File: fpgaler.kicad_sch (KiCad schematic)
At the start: 66 parts, among them J1 USB_C_Receptacle_USB2.0, J2 BATT, J3 JTAG, J4 FTDI_RST, J5 VGA, J6 DB9 Expander, SW1 RotaryEncoder_Switch, SW2 RotaryEncoder_Switch, SW3 K1, SW4 K2, SW5 PROGRAMN, SW6 K3, SW7 FPGA GSRN, SW8 K4

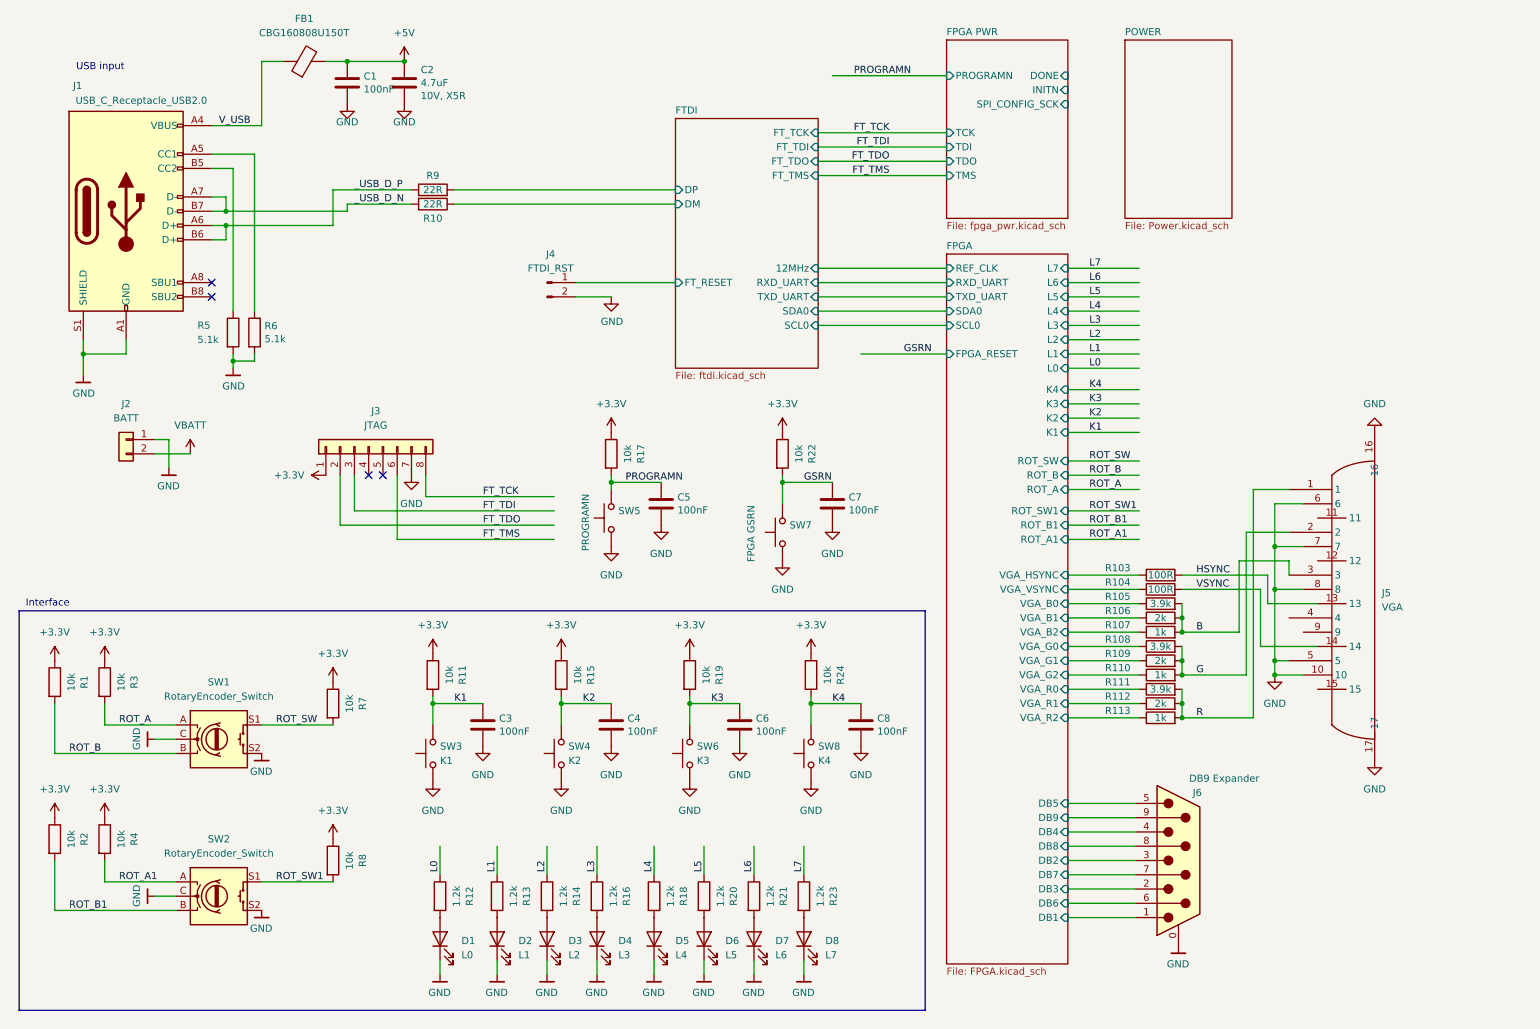
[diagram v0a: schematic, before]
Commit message: Place db9, encoder, btn and leds. Continue routing.
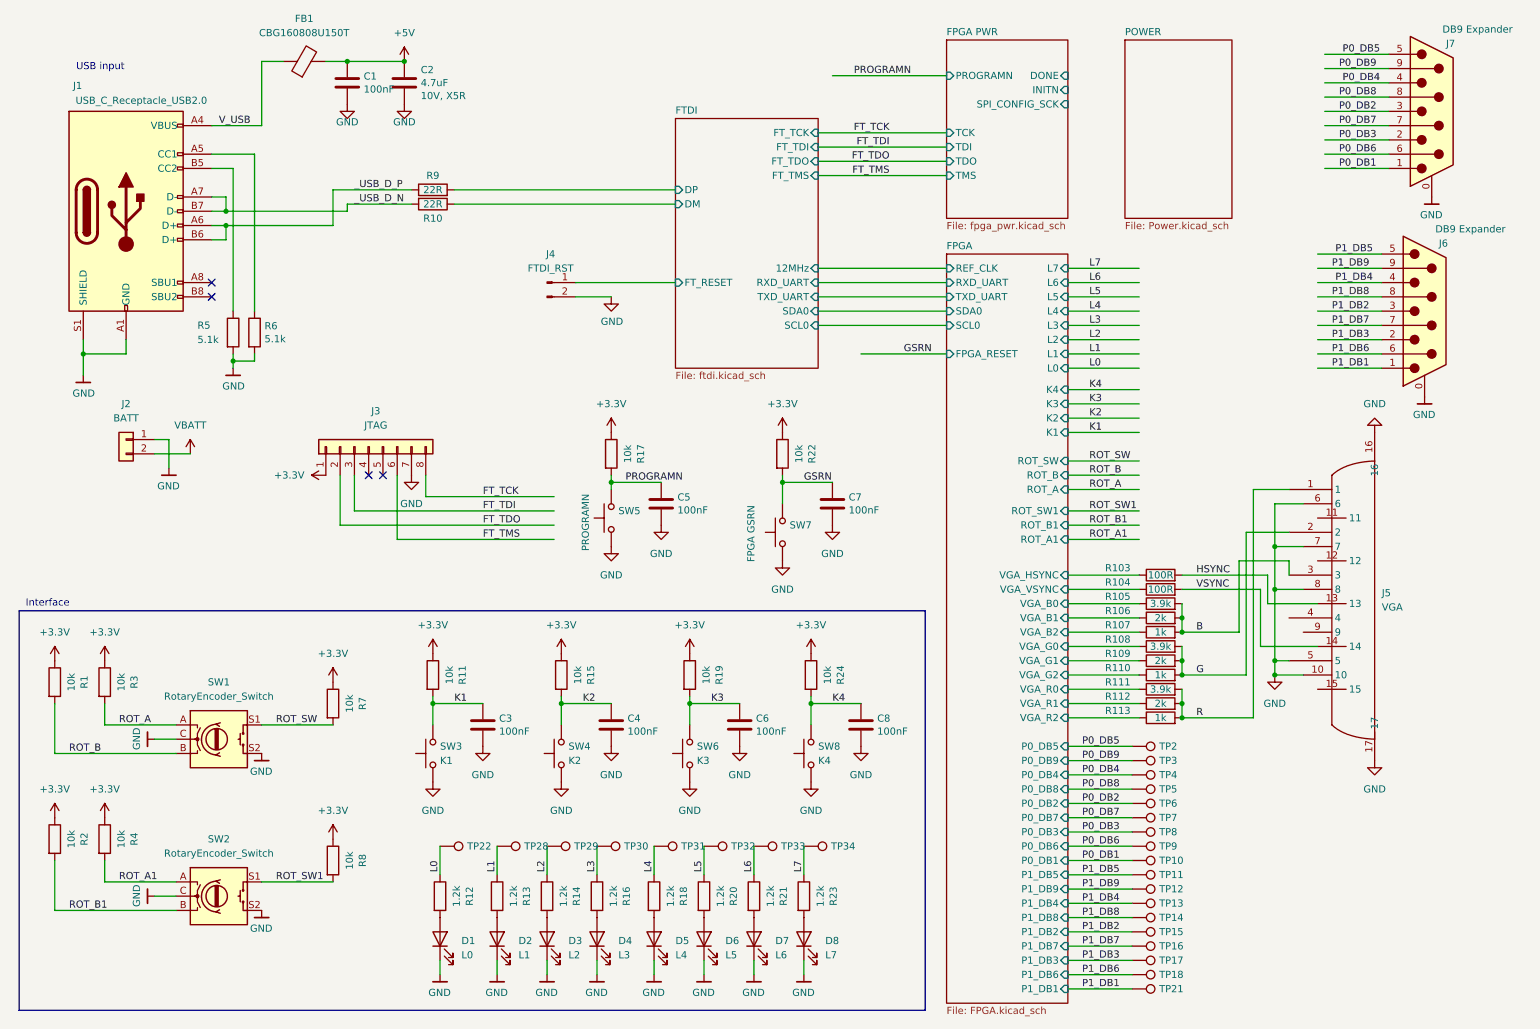
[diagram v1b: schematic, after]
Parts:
- added J7: DB9 Expander, Connector_Dsub:DSUB-9_Pins_Horizontal_P2.77x2.84mm_EdgePinOffset4.94mm_Housed_MountingHolesOffset4.94mm, symbol Connector:DE9_Pins_MountingHoles
- added TP10, TP11, TP12, TP13, TP14, TP15, TP16, TP17, TP18, TP2, TP21, TP22, TP28, TP29, TP3, TP30, TP31, TP32, TP33, TP34, TP4, TP5, TP6, TP7, TP8, TP9: TestPoint, TestPoint:TestPoint_THTPad_D1.5mm_Drill0.7mm, symbol Connector:TestPoint
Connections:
- net GND: now also J7.0 (PAD)
- net L0: now also TP22.1
- net L1: now also TP28.1
- net L2: now also TP29.1
- net L3: now also TP30.1
- net L4: now also TP31.1
- net L5: now also TP32.1
- net L6: now also TP33.1
- net L7: now also TP34.1
- net FPGA/DB1 renamed P1_DB1
- net P1_DB1: now also TP21.1
- net FPGA/DB2 renamed P1_DB2
- net P1_DB2: now also TP15.1
- net FPGA/DB3 renamed P1_DB3
- net P1_DB3: now also TP17.1
- net FPGA/DB4 renamed P1_DB4
- net P1_DB4: now also TP13.1
- net FPGA/DB5 renamed P1_DB5
- net P1_DB5: now also TP11.1
- net FPGA/DB6 renamed P1_DB6
- net P1_DB6: now also TP18.1
- net FPGA/DB7 renamed P1_DB7
- net P1_DB7: now also TP16.1
- net FPGA/DB8 renamed P1_DB8
- net P1_DB8: now also TP14.1
- net FPGA/DB9 renamed P1_DB9
- net P1_DB9: now also TP12.1
- new net P0_DB1: J7.1, TP10.1
- new net P0_DB2: J7.3, TP6.1
- new net P0_DB3: J7.2, TP8.1
- new net P0_DB4: J7.4, TP4.1
- new net P0_DB5: J7.5, TP2.1
- new net P0_DB6: J7.6, TP9.1
- new net P0_DB7: J7.7, TP7.1
- new net P0_DB8: J7.8, TP5.1
- new net P0_DB9: J7.9, TP3.1
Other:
- sheet FPGA ports: added P0_DB1, P0_DB2, P0_DB3, P0_DB4, P0_DB5, P0_DB6, P0_DB7, P0_DB8, P0_DB9, P1_DB1, P1_DB2, P1_DB3, P1_DB4, P1_DB5, P1_DB6, P1_DB7, P1_DB8, P1_DB9; removed DB1, DB2, DB3, DB4, DB5, DB6, DB7, DB8, DB9
- moved on the sheet: J6

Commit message: continue routing
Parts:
- removed J2: BATT, Connector_JST:JST_PH_S2B-PH-K_1x02_P2.00mm_Horizontal, symbol Connector_Generic:Conn_01x02
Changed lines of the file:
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@@
 	(wire
 		(pts
-			(xy 41.91 92.71) (xy 39.37 92.71)
-		)
-		(stroke
-			(width 0)
-			(type default)
-		)
-	)
-	(wire
-		(pts
 			(xy 201.93 134.62) (xy 214.63 134.62)
 		)
@@
 	(wire
 		(pts
-			(xy 45.72 95.25) (xy 39.37 95.25)
-		)
-		(stroke
-			(width 0)
-			(type default)
-		)
-	)
-	(wire
-		(pts
 			(xy 238.76 119.38) (xy 243.84 119.38)
 		)
@@
 	(wire
 		(pts
-			(xy 41.91 92.71) (xy 41.91 97.79)
-		)
-		(stroke
-			(width 0)
-			(type default)
-		)
-	)
-	(wire
-		(pts
 			(xy 222.25 121.92) (xy 222.25 124.46)
 		)
@@
 	)
 	(symbol
-		(lib_name "GND_2")
-		(lib_id "gkl_power:GND")
-		(at 41.91 97.79 0)
-		(mirror y)
-		(unit 1)
-		(exclude_from_sim no)
-		(in_bom yes)
-		(on_board yes)
-		(dnp no)
-		(property "Reference" "#PWR08"
-			(at 41.91 104.14 0)
-			(effects
-				(font
-					(size 1.27 1.27)
-				)
-				(hide yes)
-			)
-		)
-		(property "Value" "GND"
-			(at 41.8338 100.9904 0)
-			(effects
-				(font
-					(size 1.27 1.27)
-				)
-			)
-		)
-		(property "Footprint" ""
-			(at 44.45 106.68 0)
-			(effects
-				(font
-					(size 1.27 1.27)
-				)
-				(hide yes)
-			)
-		)
-		(property "Datasheet" ""
-			(at 41.91 97.79 0)
-			(effects
-				(font
-					(size 1.27 1.27)
-				)
-				(hide yes)
-			)
-		)
-		(property "Description" ""
-			(at 41.91 97.79 0)
-			(effects
-				(font
-					(size 1.27 1.27)
-				)
-			)
-		)
-		(pin "1"
-		)
-		(instances
-			(project "fpgaler"
-				(path "/d6c42660-1080-4fbd-a2d9-2a0cd6b4e770"
-					(reference "#PWR08")
-					(unit 1)
-				)
-			)
-		)
-	)
-	(symbol
 		(lib_id "gkl_power:GND")
 		(at 26.67 81.28 0)
@@
 	)
 	(symbol
-		(lib_id "Connector_Generic:Conn_01x02")
-		(at 34.29 92.71 0)
-		(mirror y)
-		(unit 1)
-		(exclude_from_sim no)
-		(in_bom yes)
-		(on_board yes)
-		(dnp no)
-		(fields_autoplaced yes)
-		(property "Reference" "J2"
-			(at 34.29 86.36 0)
-			(effects
-				(font
-					(size 1.27 1.27)
-				)
-			)
-		)
-		(property "Value" "BATT"
-			(at 34.29 88.9 0)
-			(effects
-				(font
-					(size 1.27 1.27)
-				)
-			)
-		)
-		(property "Footprint" "Connector_JST:JST_PH_S2B-PH-K_1x02_P2.00mm_Horizontal"
-			(at 34.29 92.71 0)
-			(effects
-				(font
-					(size 1.27 1.27)
-				)
-				(hide yes)
-			)
-		)
-		(property "Datasheet" "~"
-			(at 34.29 92.71 0)
-			(effects
-				(font
-					(size 1.27 1.27)
-				)
-				(hide yes)
-			)
-		)
-		(property "Description" "Generic connector, single row, 01x02, script generated (kicad-library-utils/schlib/autogen/connector/)"
-			(at 34.29 92.71 0)
-			(effects
-				(font
-					(size 1.27 1.27)
-				)
-				(hide yes)
-			)
-		)
-		(property "LCSC" "C173752"
-			(at 34.29 92.71 0)
-			(effects
-				(font
-					(size 1.27 1.27)
-				)
-				(hide yes)
-			)
-		)
-		(pin "1"
-		)
-		(pin "2"
-		)
-		(instances
-			(project ""
-				(path "/d6c42660-1080-4fbd-a2d9-2a0cd6b4e770"
-					(reference "J2")
-					(unit 1)
-				)
-			)
-		)
-	)
-	(symbol
 		(lib_id "Device:R")
 		(at 21.59 163.83 0)
@@
 					(unit 1)
 				)
-			)
-		)
-	)
-	(symbol
-		(lib_id "power:+3.3V")
-		(at 45.72 95.25 0)
-		(unit 1)
-		(exclude_from_sim no)
-		(in_bom yes)
-		(on_board yes)
-		(dnp no)
-		(fields_autoplaced yes)
-		(property "Reference" "#PWR09"
-			(at 45.72 99.06 0)
-			(effects
-				(font
-					(size 1.27 1.27)
-				)
-				(hide yes)
-			)
-		)
-		(property "Value" "VBATT"
-			(at 45.72 90.17 0)
-			(effects
-				(font
-					(size 1.27 1.27)
-				)
-			)
-		)
-		(property "Footprint" ""
-			(at 45.72 95.25 0)
-			(effects
-				(font
-					(size 1.27 1.27)
-				)
-				(hide yes)
-			)
-		)
-		(property "Datasheet" ""
-			(at 45.72 95.25 0)
-			(effects
-				(font
-					(size 1.27 1.27)
-				)
-				(hide yes)
-			)
-		)
-		(property "Description" "Power symbol creates a global label with name \"+3.3V\""
-			(at 45.72 95.25 0)
-			(effects
-				(font
-					(size 1.27 1.27)
-				)
-				(hide yes)
-			)
-		)
-		(pin "1"
-		)
-		(instances
-			(project "fpgaler"
-				(path "/d6c42660-1080-4fbd-a2d9-2a0cd6b4e770"
-					(reference "#PWR09")
-					(unit 1)
-				)

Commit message: Start routing pwr
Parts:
- added TP1, TP19, TP20, TP23, TP24, TP25: TestPoint, TestPoint:TestPoint_THTPad_D1.5mm_Drill0.7mm, symbol Connector:TestPoint
- FB1: value CBG160808U150T -> 15Ω@100MHz; footprint Inductor_SMD:L_0603_1608Metric -> Inductor_SMD:L_0603_1608Metric_Pad1.05x0.95mm_HandSolder
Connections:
- net +3.3V: now also TP1.1, TP20.1
- net GND: now also TP19.1, TP23.1
- net FTDI/DM renamed FTDI/D_N
- net FTDI/DP renamed FTDI/D_P
- net _USB_D_N renamed USB_N
- net _USB_D_P renamed USB_P
- new net +2.5V: TP24.1, TP25.1
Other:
- sheet FTDI ports: added D_N, D_P; removed DM, DP

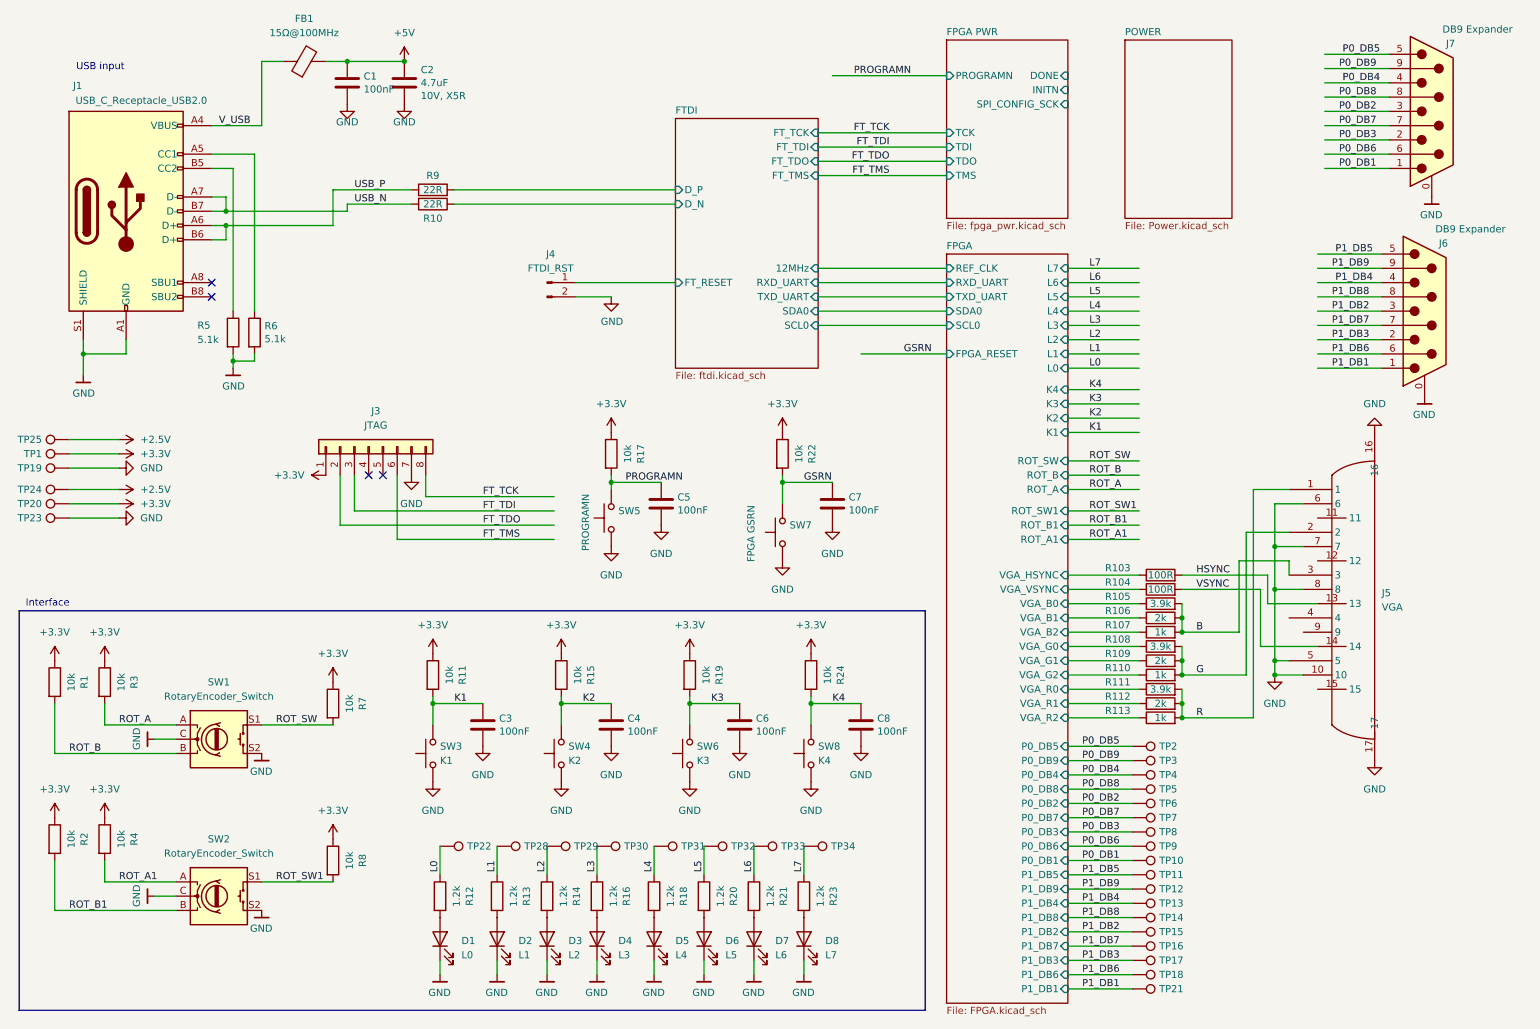
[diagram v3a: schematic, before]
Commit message: Fix dcr for schematics
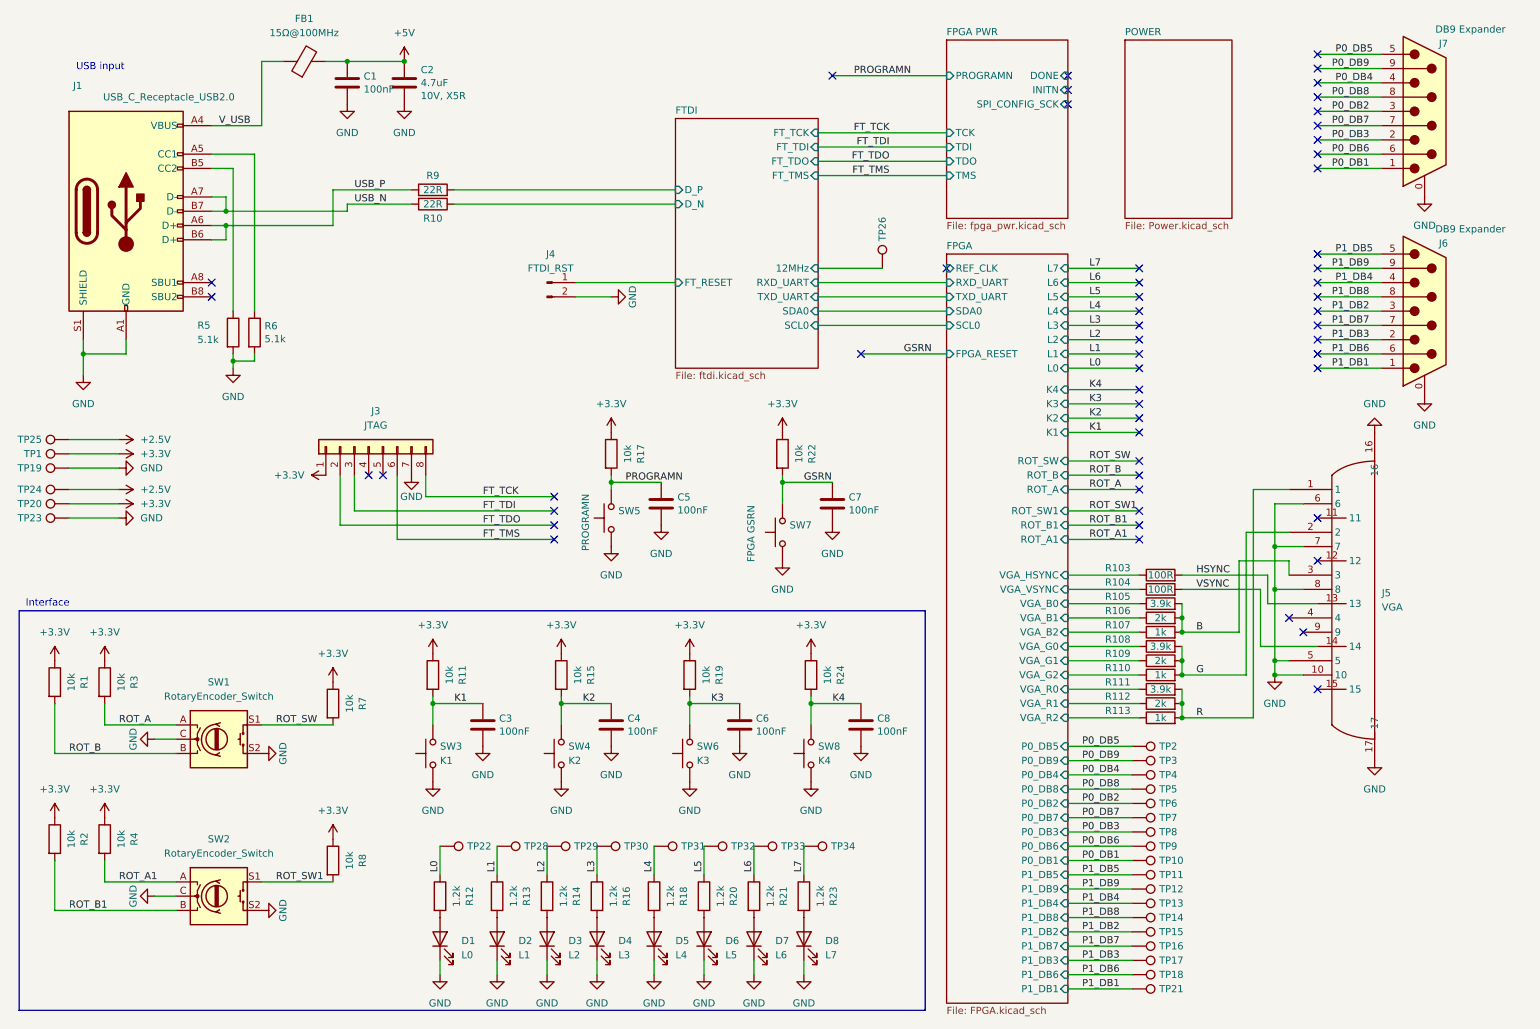
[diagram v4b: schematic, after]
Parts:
- added TP26: TestPoint, TestPoint:TestPoint_THTPad_D1.5mm_Drill0.7mm, symbol Connector:TestPoint
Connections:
- new net FTDI/12MHz: TP26.1
- no-connect marks 4 -> 55
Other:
- moved on the sheet: J7
